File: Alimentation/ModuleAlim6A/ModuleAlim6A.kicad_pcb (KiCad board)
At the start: 2 copper layers, 40 x 52 mm, 12 parts, among them J1 Inhibit, J2 Alim. IN / OUT, U1 PTN78020W_EUK-7

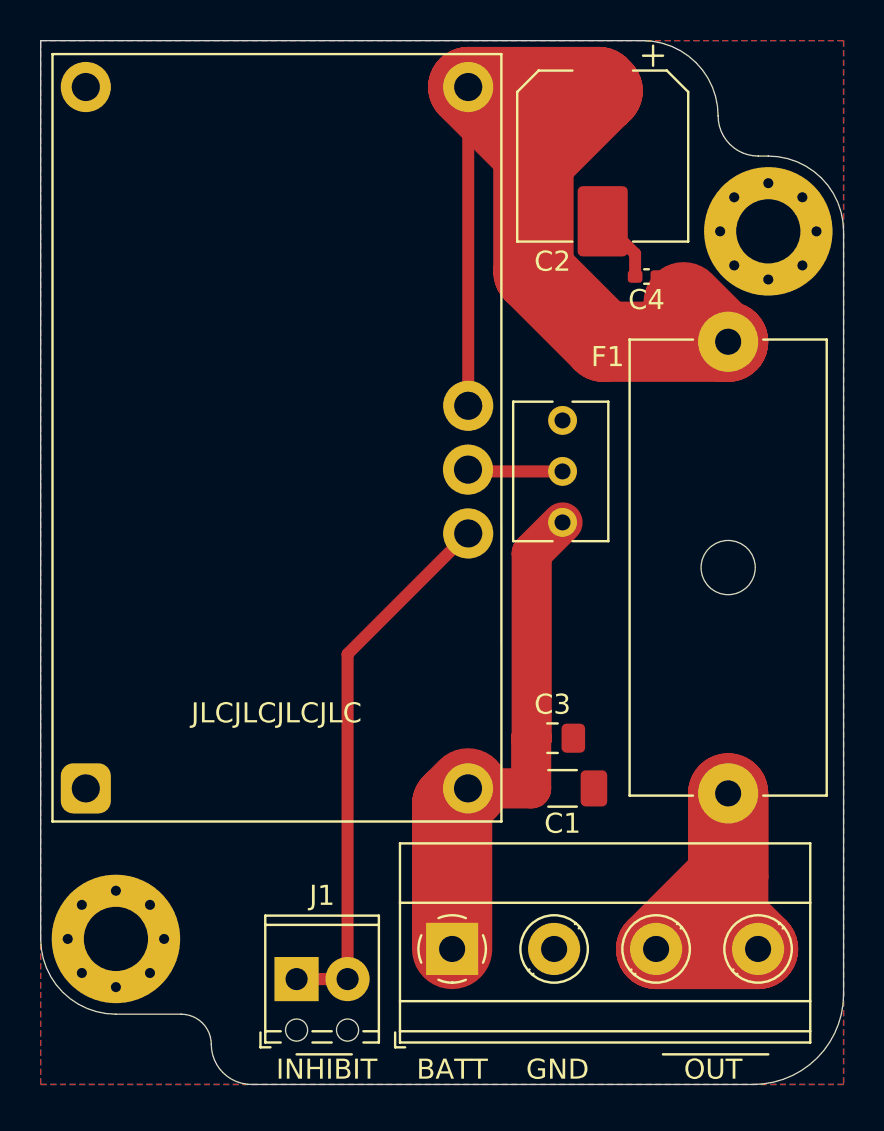
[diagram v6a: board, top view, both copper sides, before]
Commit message: Upgrade to KicCad 8
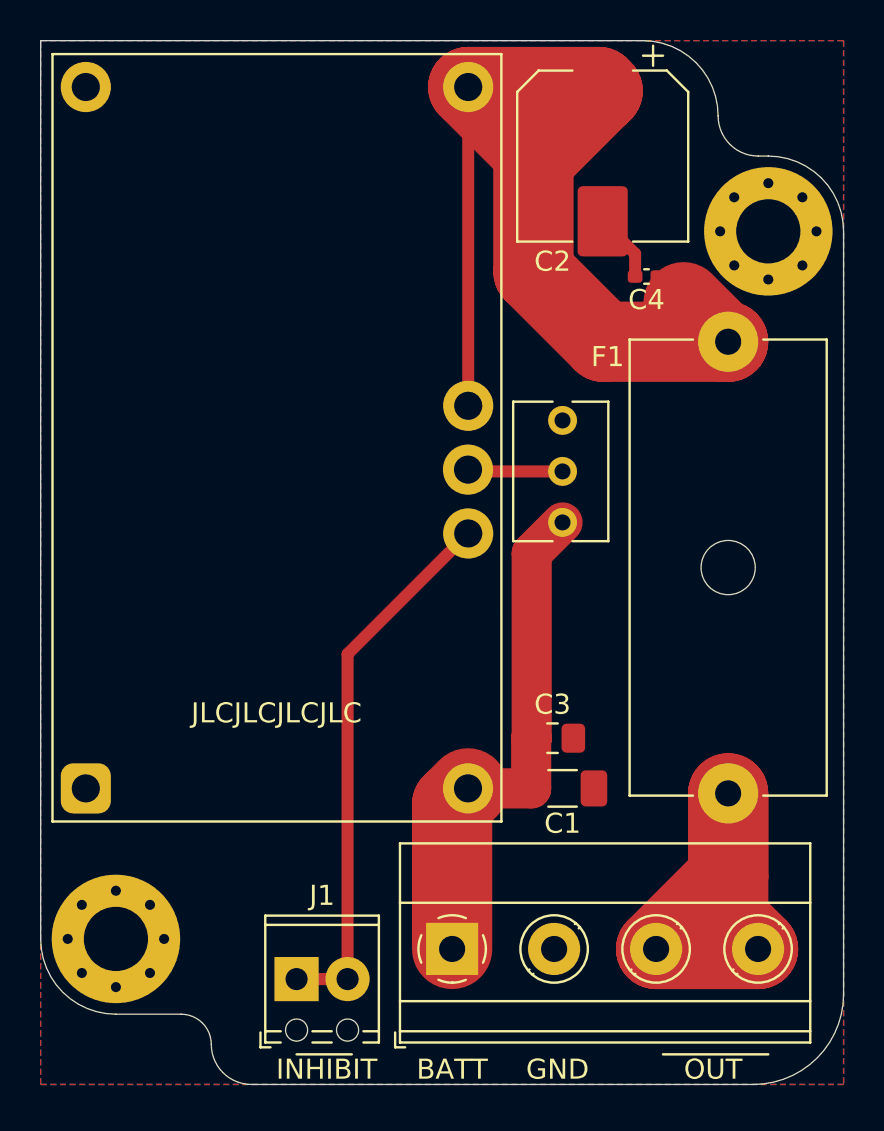
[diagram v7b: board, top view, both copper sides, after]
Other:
- net class Default removed
